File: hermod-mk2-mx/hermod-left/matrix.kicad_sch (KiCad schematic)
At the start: 76 parts

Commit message: UPdated Hermod Mk 2 to have ks33 and choc v2 footprints
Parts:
- CH1, CH10, CH11, CH12, CH13, CH14, CH15, CH17, CH18, CH19, CH20, CH21, CH22, CH24, CH25, CH26, CH27, CH28, CH29, CH3, CH31, CH32, CH33, CH34, CH35, CH4, CH5, CH6, CH7, CH8: footprint Gateron_KS33_Hotswap:Gateron-KS33-Hotswap-1U -> ModHob:KS33_Choc-v2_HS_1U
- CH16, CH2, CH23, CH30, CH36, CH37, CH38, CH9: footprint Gateron_KS33_Hotswap:Gateron-KS33-Hotswap-1.5U -> ModHob:KS33_Choc-v2_HS_1.5U
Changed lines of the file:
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@@
 			)
 		)
-		(property "Footprint" "Gateron_KS33_Hotswap:Gateron-KS33-Hotswap-1U"
+		(property "Footprint" "ModHob:KS33_Choc-v2_HS_1U"
 			(at 147.32 162.56 0)
 			(effects
@@
 			)
 		)
-		(property "Footprint" "Gateron_KS33_Hotswap:Gateron-KS33-Hotswap-1U"
+		(property "Footprint" "ModHob:KS33_Choc-v2_HS_1U"
 			(at 236.22 95.25 0)
 			(effects
@@
 			)
 		)
-		(property "Footprint" "Gateron_KS33_Hotswap:Gateron-KS33-Hotswap-1U"
+		(property "Footprint" "ModHob:KS33_Choc-v2_HS_1U"
 			(at 182.88 118.11 0)
 			(effects
@@
 			)
 		)
-		(property "Footprint" "Gateron_KS33_Hotswap:Gateron-KS33-Hotswap-1.5U"
+		(property "Footprint" "ModHob:KS33_Choc-v2_HS_1.5U"
 			(at 165.1 95.25 0)
 			(effects
@@
 			)
 		)
-		(property "Footprint" "Gateron_KS33_Hotswap:Gateron-KS33-Hotswap-1U"
+		(property "Footprint" "ModHob:KS33_Choc-v2_HS_1U"
 			(at 236.22 139.7 0)
 			(effects
@@
 			)
 		)
-		(property "Footprint" "Gateron_KS33_Hotswap:Gateron-KS33-Hotswap-1U"
+		(property "Footprint" "ModHob:KS33_Choc-v2_HS_1U"
 			(at 236.22 162.56 0)
 			(effects
@@
 			)
 		)
-		(property "Footprint" "Gateron_KS33_Hotswap:Gateron-KS33-Hotswap-1U"
+		(property "Footprint" "ModHob:KS33_Choc-v2_HS_1U"
 			(at 200.66 72.39 0)
 			(effects
@@
 			)
 		)
-		(property "Footprint" "Gateron_KS33_Hotswap:Gateron-KS33-Hotswap-1U"
+		(property "Footprint" "ModHob:KS33_Choc-v2_HS_1U"
 			(at 254 139.7 0)
 			(effects
@@
 			)
 		)
-		(property "Footprint" "Gateron_KS33_Hotswap:Gateron-KS33-Hotswap-1U"
+		(property "Footprint" "ModHob:KS33_Choc-v2_HS_1U"
 			(at 147.32 118.11 0)
 			(effects
@@
 			)
 		)
-		(property "Footprint" "Gateron_KS33_Hotswap:Gateron-KS33-Hotswap-1U"
+		(property "Footprint" "ModHob:KS33_Choc-v2_HS_1U"
 			(at 218.44 139.7 0)
 			(effects
@@
 			)
 		)
-		(property "Footprint" "Gateron_KS33_Hotswap:Gateron-KS33-Hotswap-1.5U"
+		(property "Footprint" "ModHob:KS33_Choc-v2_HS_1.5U"
 			(at 165.1 162.56 0)
 			(effects
@@
 			)
 		)
-		(property "Footprint" "Gateron_KS33_Hotswap:Gateron-KS33-Hotswap-1U"
+		(property "Footprint" "ModHob:KS33_Choc-v2_HS_1U"
 			(at 236.22 118.11 0)
 			(effects
@@
 			)
 		)
-		(property "Footprint" "Gateron_KS33_Hotswap:Gateron-KS33-Hotswap-1U"
+		(property "Footprint" "ModHob:KS33_Choc-v2_HS_1U"
 			(at 254 162.56 0)
 			(effects
@@
 			)
 		)
-		(property "Footprint" "Gateron_KS33_Hotswap:Gateron-KS33-Hotswap-1.5U"
+		(property "Footprint" "ModHob:KS33_Choc-v2_HS_1.5U"
 			(at 165.1 72.39 0)
 			(effects
@@
 			)
 		)
-		(property "Footprint" "Gateron_KS33_Hotswap:Gateron-KS33-Hotswap-1.5U"
+		(property "Footprint" "ModHob:KS33_Choc-v2_HS_1.5U"
 			(at 218.44 186.69 0)
 			(effects
@@
 			)
 		)
-		(property "Footprint" "Gateron_KS33_Hotswap:Gateron-KS33-Hotswap-1U"
+		(property "Footprint" "ModHob:KS33_Choc-v2_HS_1U"
 			(at 147.32 72.39 0)
 			(effects
@@
 			)
 		)
-		(property "Footprint" "Gateron_KS33_Hotswap:Gateron-KS33-Hotswap-1.5U"
+		(property "Footprint" "ModHob:KS33_Choc-v2_HS_1.5U"
 			(at 254 186.69 0)
 			(effects
@@
 			)
 		)
-		(property "Footprint" "Gateron_KS33_Hotswap:Gateron-KS33-Hotswap-1U"
+		(property "Footprint" "ModHob:KS33_Choc-v2_HS_1U"
 			(at 218.44 118.11 0)
 			(effects
@@
 			)
 		)
-		(property "Footprint" "Gateron_KS33_Hotswap:Gateron-KS33-Hotswap-1U"
+		(property "Footprint" "ModHob:KS33_Choc-v2_HS_1U"
 			(at 254 72.39 0)
 			(effects
@@
 			)
 		)
-		(property "Footprint" "Gateron_KS33_Hotswap:Gateron-KS33-Hotswap-1U"
+		(property "Footprint" "ModHob:KS33_Choc-v2_HS_1U"
 			(at 200.66 162.56 0)
 			(effects
@@
 			)
 		)
-		(property "Footprint" "Gateron_KS33_Hotswap:Gateron-KS33-Hotswap-1U"
+		(property "Footprint" "ModHob:KS33_Choc-v2_HS_1U"
 			(at 200.66 118.11 0)
 			(effects
@@
 			)
 		)
-		(property "Footprint" "Gateron_KS33_Hotswap:Gateron-KS33-Hotswap-1U"
+		(property "Footprint" "ModHob:KS33_Choc-v2_HS_1U"
 			(at 218.44 95.25 0)
 			(effects
@@
 			)
 		)
-		(property "Footprint" "Gateron_KS33_Hotswap:Gateron-KS33-Hotswap-1.5U"
+		(property "Footprint" "ModHob:KS33_Choc-v2_HS_1.5U"
 			(at 165.1 139.7 0)
 			(effects
@@
 			)
 		)
-		(property "Footprint" "Gateron_KS33_Hotswap:Gateron-KS33-Hotswap-1U"
+		(property "Footprint" "ModHob:KS33_Choc-v2_HS_1U"
 			(at 200.66 139.7 0)
 			(effects
@@
 			)
 		)
-		(property "Footprint" "Gateron_KS33_Hotswap:Gateron-KS33-Hotswap-1U"
+		(property "Footprint" "ModHob:KS33_Choc-v2_HS_1U"
 			(at 254 95.25 0)
 			(effects
@@
 			)
 		)
-		(property "Footprint" "Gateron_KS33_Hotswap:Gateron-KS33-Hotswap-1U"
+		(property "Footprint" "ModHob:KS33_Choc-v2_HS_1U"
 			(at 236.22 72.39 0)
 			(effects
@@
 			)
 		)
-		(property "Footprint" "Gateron_KS33_Hotswap:Gateron-KS33-Hotswap-1.5U"
+		(property "Footprint" "ModHob:KS33_Choc-v2_HS_1.5U"
 			(at 165.1 118.11 0)
 			(effects
@@
 			)
 		)
-		(property "Footprint" "Gateron_KS33_Hotswap:Gateron-KS33-Hotswap-1U"
+		(property "Footprint" "ModHob:KS33_Choc-v2_HS_1U"
 			(at 182.88 72.39 0)
 			(effects
@@
 			)
 		)
-		(property "Footprint" "Gateron_KS33_Hotswap:Gateron-KS33-Hotswap-1.5U"
+		(property "Footprint" "ModHob:KS33_Choc-v2_HS_1.5U"
 			(at 236.22 186.69 0)
 			(effects
@@
 			)
 		)
-		(property "Footprint" "Gateron_KS33_Hotswap:Gateron-KS33-Hotswap-1U"
+		(property "Footprint" "ModHob:KS33_Choc-v2_HS_1U"
 			(at 147.32 139.7 0)
 			(effects
@@
 			)
 		)
-		(property "Footprint" "Gateron_KS33_Hotswap:Gateron-KS33-Hotswap-1U"
+		(property "Footprint" "ModHob:KS33_Choc-v2_HS_1U"
 			(at 254 118.11 0)
 			(effects
@@
 			)
 		)
-		(property "Footprint" "Gateron_KS33_Hotswap:Gateron-KS33-Hotswap-1U"
+		(property "Footprint" "ModHob:KS33_Choc-v2_HS_1U"
 			(at 182.88 162.56 0)
 			(effects
@@
 			)
 		)
-		(property "Footprint" "Gateron_KS33_Hotswap:Gateron-KS33-Hotswap-1U"
+		(property "Footprint" "ModHob:KS33_Choc-v2_HS_1U"
 			(at 218.44 72.39 0)
 			(effects
@@
 			)
 		)
-		(property "Footprint" "Gateron_KS33_Hotswap:Gateron-KS33-Hotswap-1U"
+		(property "Footprint" "ModHob:KS33_Choc-v2_HS_1U"
 			(at 182.88 139.7 0)
 			(effects
@@
 			)
 		)
-		(property "Footprint" "Gateron_KS33_Hotswap:Gateron-KS33-Hotswap-1U"
+		(property "Footprint" "ModHob:KS33_Choc-v2_HS_1U"
 			(at 147.32 95.25 0)
 			(effects
@@
 			)
 		)
-		(property "Footprint" "Gateron_KS33_Hotswap:Gateron-KS33-Hotswap-1U"
+		(property "Footprint" "ModHob:KS33_Choc-v2_HS_1U"
 			(at 200.66 95.25 0)
 			(effects
@@
 			)
 		)
-		(property "Footprint" "Gateron_KS33_Hotswap:Gateron-KS33-Hotswap-1U"
+		(property "Footprint" "ModHob:KS33_Choc-v2_HS_1U"
 			(at 218.44 162.56 0)
 			(effects
@@
 			)
 		)
-		(property "Footprint" "Gateron_KS33_Hotswap:Gateron-KS33-Hotswap-1U"
+		(property "Footprint" "ModHob:KS33_Choc-v2_HS_1U"
 			(at 182.88 95.25 0)
 			(effects

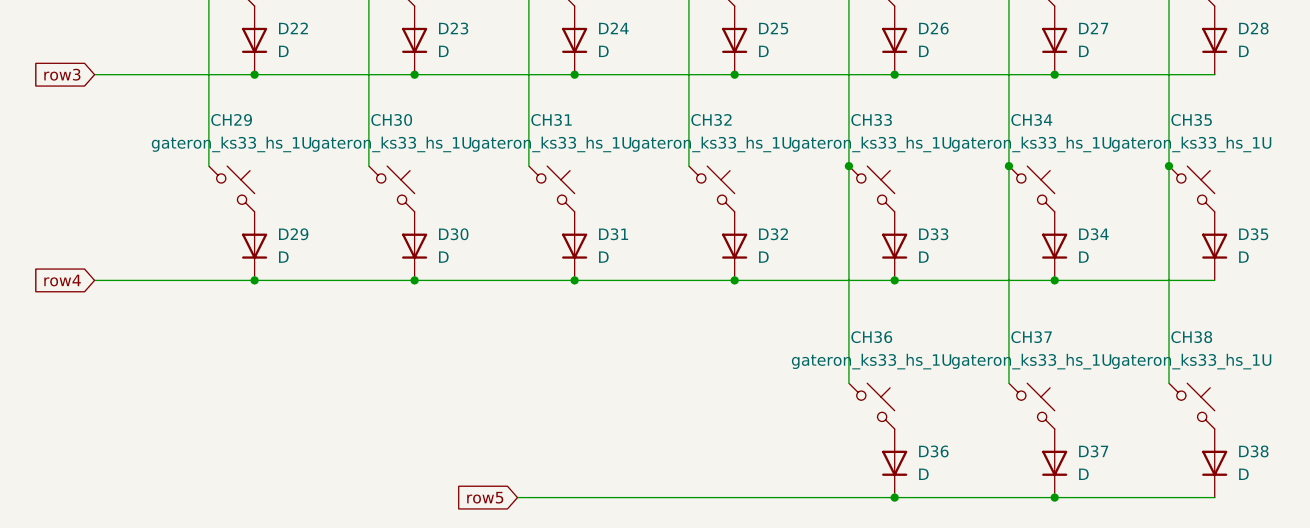
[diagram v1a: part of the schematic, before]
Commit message: Added switches to hermod 3 and updated mist thumb spacing
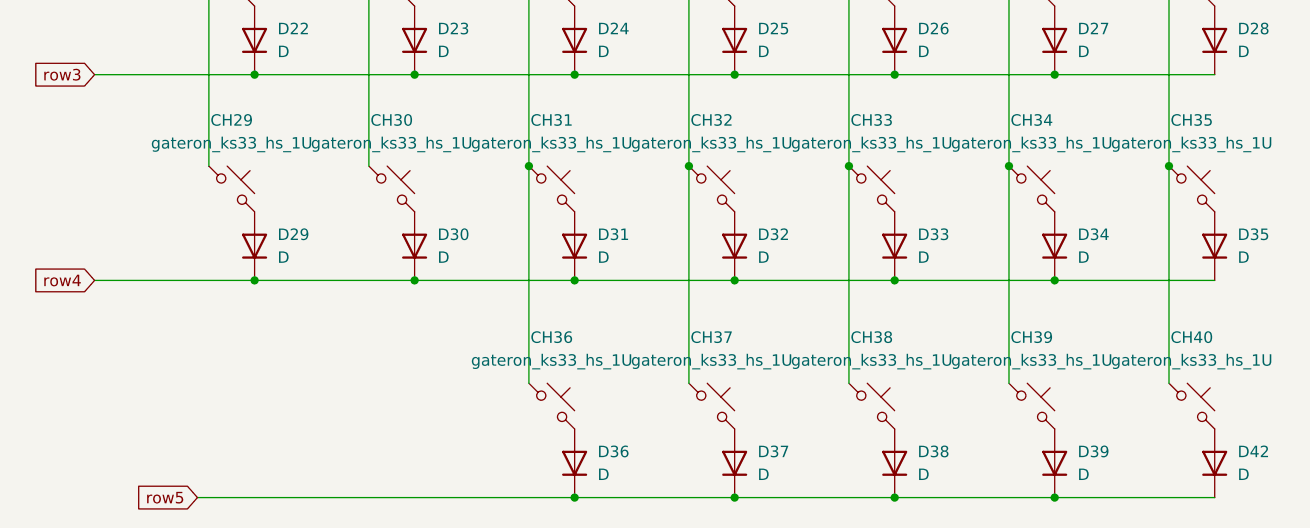
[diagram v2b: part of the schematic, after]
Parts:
- added CH39, CH40: gateron_ks33_hs_1U, ModHob:KS33_Choc-v2_HS_1.5U, symbol PCM_marbastlib-choc:choc_v1_SW_HS_CPG135001S30
- added D39, D42: D, Diode_SMD:D_SOD-123, symbol Device:D
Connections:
- net col2: now also CH36.1
- net col3: now also CH37.1
- net col4: now also CH38.1; no longer CH36.1
- net col5: now also CH39.1; no longer CH37.1
- net col6: now also CH40.1; no longer CH38.1
- net row5: now also D39.1 (K), D42.1 (K)
- new net: CH39.2, D39.2 (A)
- new net: CH40.2, D42.2 (A)
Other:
- moved on the sheet: CH36, CH37, CH38, D36, D37, D38

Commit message: Fixed spacing issues
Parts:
- CH39, CH40: footprint ModHob:KS33_Choc-v2_HS_1.5U -> ModHob:KS33_Choc-v2_HS_1U
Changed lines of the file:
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@@
 			)
 		)
-		(property "Footprint" "ModHob:KS33_Choc-v2_HS_1.5U"
+		(property "Footprint" "ModHob:KS33_Choc-v2_HS_1U"
 			(at 236.22 186.69 0)
 			(effects
@@
 			)
 		)
-		(property "Footprint" "ModHob:KS33_Choc-v2_HS_1.5U"
+		(property "Footprint" "ModHob:KS33_Choc-v2_HS_1U"
 			(at 254 186.69 0)
 			(effects
